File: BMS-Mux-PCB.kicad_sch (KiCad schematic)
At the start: 54 parts, among them J1 Conn_02x08_Counter_Clockwise, J2 Conn_02x08_Counter_Clockwise, J3 Conn_02x09_Top_Bottom, J4 Conn_01x18, J5 Conn_01x02, J6 Conn_02x10_Odd_Even, Q1 BSS123, Q2 BSS123, U1 74CBTLV3257, U2 74CBTLV3257, U3 TEC2-4812WI, U4 TEC2-4810WI

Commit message: V1 almost done - touching up silkscreen
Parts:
- renumbered F16 to F1, F7 to F10, F6 to F11, F5 to F12, F4 to F13, F3 to F14, F2 to F15, F1 to F16, F15 to F2, F14 to F3, F13 to F4, F12 to F5, F11 to F6, F10 to F7, F9 to F8, F8 to F9
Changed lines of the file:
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@@
 		(on_board yes)
 		(dnp no)
-		(property "Reference" "F13"
+		(property "Reference" "F4"
 			(at 99.06 189.484 90)
 			(effects
@@
 			(project "BMS-Mux-PCB"
 				(path "/a2925814-5dc3-4888-bdb8-1bf38cbb6bf2"
-					(reference "F13")
+					(reference "F4")
 					(unit 1)
 				)
@@
 		(on_board yes)
 		(dnp no)
-		(property "Reference" "F9"
+		(property "Reference" "F8"
 			(at 99.06 179.324 90)
 			(effects
@@
 			(project "BMS-Mux-PCB"
 				(path "/a2925814-5dc3-4888-bdb8-1bf38cbb6bf2"
-					(reference "F9")
+					(reference "F8")
 					(unit 1)
 				)
@@
 		(on_board yes)
 		(dnp no)
-		(property "Reference" "F11"
+		(property "Reference" "F6"
 			(at 99.06 184.404 90)
 			(effects
@@
 			(project "BMS-Mux-PCB"
 				(path "/a2925814-5dc3-4888-bdb8-1bf38cbb6bf2"
-					(reference "F11")
+					(reference "F6")
 					(unit 1)
 				)
@@
 		(on_board yes)
 		(dnp no)
-		(property "Reference" "F6"
+		(property "Reference" "F11"
 			(at 99.06 171.704 90)
 			(effects
@@
 			(project "BMS-Mux-PCB"
 				(path "/a2925814-5dc3-4888-bdb8-1bf38cbb6bf2"
-					(reference "F6")
+					(reference "F11")
 					(unit 1)
 				)
@@
 		(on_board yes)
 		(dnp no)
-		(property "Reference" "F16"
+		(property "Reference" "F1"
 			(at 99.06 197.104 90)
 			(effects
@@
 			(project "BMS-Mux-PCB"
 				(path "/a2925814-5dc3-4888-bdb8-1bf38cbb6bf2"
-					(reference "F16")
+					(reference "F1")
 					(unit 1)
 				)
@@
 		(on_board yes)
 		(dnp no)
-		(property "Reference" "F8"
+		(property "Reference" "F9"
 			(at 99.06 176.784 90)
 			(effects
@@
 			(project "BMS-Mux-PCB"
 				(path "/a2925814-5dc3-4888-bdb8-1bf38cbb6bf2"
-					(reference "F8")
+					(reference "F9")
 					(unit 1)
 				)
@@
 		(on_board yes)
 		(dnp no)
-		(property "Reference" "F1"
+		(property "Reference" "F16"
 			(at 99.06 159.004 90)
 			(effects
@@
 			(project "BMS-Mux-PCB"
 				(path "/a2925814-5dc3-4888-bdb8-1bf38cbb6bf2"
-					(reference "F1")
+					(reference "F16")
 					(unit 1)
 				)
@@
 		(on_board yes)
 		(dnp no)
-		(property "Reference" "F7"
+		(property "Reference" "F10"
 			(at 99.06 174.244 90)
 			(effects
@@
 			(project "BMS-Mux-PCB"
 				(path "/a2925814-5dc3-4888-bdb8-1bf38cbb6bf2"
-					(reference "F7")
+					(reference "F10")
 					(unit 1)
 				)
@@
 		(on_board yes)
 		(dnp no)
-		(property "Reference" "F2"
+		(property "Reference" "F15"
 			(at 99.06 161.544 90)
 			(effects
@@
 			(project "BMS-Mux-PCB"
 				(path "/a2925814-5dc3-4888-bdb8-1bf38cbb6bf2"
-					(reference "F2")
+					(reference "F15")
 					(unit 1)
 				)
@@
 		(on_board yes)
 		(dnp no)
-		(property "Reference" "F5"
+		(property "Reference" "F12"
 			(at 99.06 169.164 90)
 			(effects
@@
 			(project "BMS-Mux-PCB"
 				(path "/a2925814-5dc3-4888-bdb8-1bf38cbb6bf2"
-					(reference "F5")
+					(reference "F12")
 					(unit 1)
 				)
@@
 		(on_board yes)
 		(dnp no)
-		(property "Reference" "F10"
+		(property "Reference" "F7"
 			(at 99.06 181.864 90)
 			(effects
@@
 			(project "BMS-Mux-PCB"
 				(path "/a2925814-5dc3-4888-bdb8-1bf38cbb6bf2"
-					(reference "F10")
+					(reference "F7")
 					(unit 1)
 				)
@@
 		(on_board yes)
 		(dnp no)
-		(property "Reference" "F14"
+		(property "Reference" "F3"
 			(at 99.06 192.024 90)
 			(effects
@@
 			(project "BMS-Mux-PCB"
 				(path "/a2925814-5dc3-4888-bdb8-1bf38cbb6bf2"
-					(reference "F14")
+					(reference "F3")
 					(unit 1)
 				)
@@
 		(on_board yes)
 		(dnp no)
-		(property "Reference" "F3"
+		(property "Reference" "F14"
 			(at 99.06 164.084 90)
 			(effects
@@
 			(project "BMS-Mux-PCB"
 				(path "/a2925814-5dc3-4888-bdb8-1bf38cbb6bf2"
-					(reference "F3")
+					(reference "F14")
 					(unit 1)
 				)
@@
 		(on_board yes)
 		(dnp no)
-		(property "Reference" "F4"
+		(property "Reference" "F13"
 			(at 99.06 166.624 90)
 			(effects
@@
 			(project "BMS-Mux-PCB"
 				(path "/a2925814-5dc3-4888-bdb8-1bf38cbb6bf2"
-					(reference "F4")
+					(reference "F13")
 					(unit 1)
 				)
@@
 		(on_board yes)
 		(dnp no)
-		(property "Reference" "F15"
+		(property "Reference" "F2"
 			(at 99.06 194.564 90)
 			(effects
@@
 			(project "BMS-Mux-PCB"
 				(path "/a2925814-5dc3-4888-bdb8-1bf38cbb6bf2"
-					(reference "F15")
+					(reference "F2")
 					(unit 1)
 				)
@@
 		(on_board yes)
 		(dnp no)
-		(property "Reference" "F12"
+		(property "Reference" "F5"
 			(at 99.06 186.944 90)
 			(effects
@@
 			(project "BMS-Mux-PCB"
 				(path "/a2925814-5dc3-4888-bdb8-1bf38cbb6bf2"
-					(reference "F12")
+					(reference "F5")
 					(unit 1)
 				)

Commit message: added some small changes for manufacturing purposes and gerber file generated
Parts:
- C1, C2: Manufacturer Part Number (none) -> CL10B104KB85PND
- C3, C4: Manufacturer Part Number (none) -> 885382208016
- F1, F10, F11, F12, F13, F14, F15, F16, F2, F3, F4, F5, F6, F7, F8, F9: Manufacturer Part Number (none) -> 0466.250NR
- H1, H2, H3, H4: now not fitted
- J1, J2: Manufacturer Part Number (none) -> 43045-1600
- J3: Manufacturer Part Number (none) -> 43045-1800
- J4: Manufacturer Part Number (none) -> 1945151 (x2)
- J5: Manufacturer Part Number (none) -> 43650-0200
- J6: Manufacturer Part Number (none) -> PH2-20-UA
- Q1, Q2: Manufacturer Part Number (none) -> BSS123L
- R1, R10, R11, R12, R13, R14, R15, R16, R2, R3, R4, R5, R6, R7, R8, R9: Manufacturer Part Number (none) -> ERA-6AEB681V
- R17, R18: Manufacturer Part Number (none) -> ERA-6AEB163V
- U1, U2: Manufacturer Part Number (none) -> SN74LV4053ADR
- U3: Manufacturer Part Number (none) -> TEC2-4812WI
- U4: Manufacturer Part Number (none) -> TEC2-4810WI
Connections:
- net +12V_ISO: now reaches J5.1 (Pin_1), U3.6 (+VOUT)
- net GND_ISO: now reaches J5.2 (Pin_2), U3.7 (-VOUT)
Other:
- moved on the sheet: J5

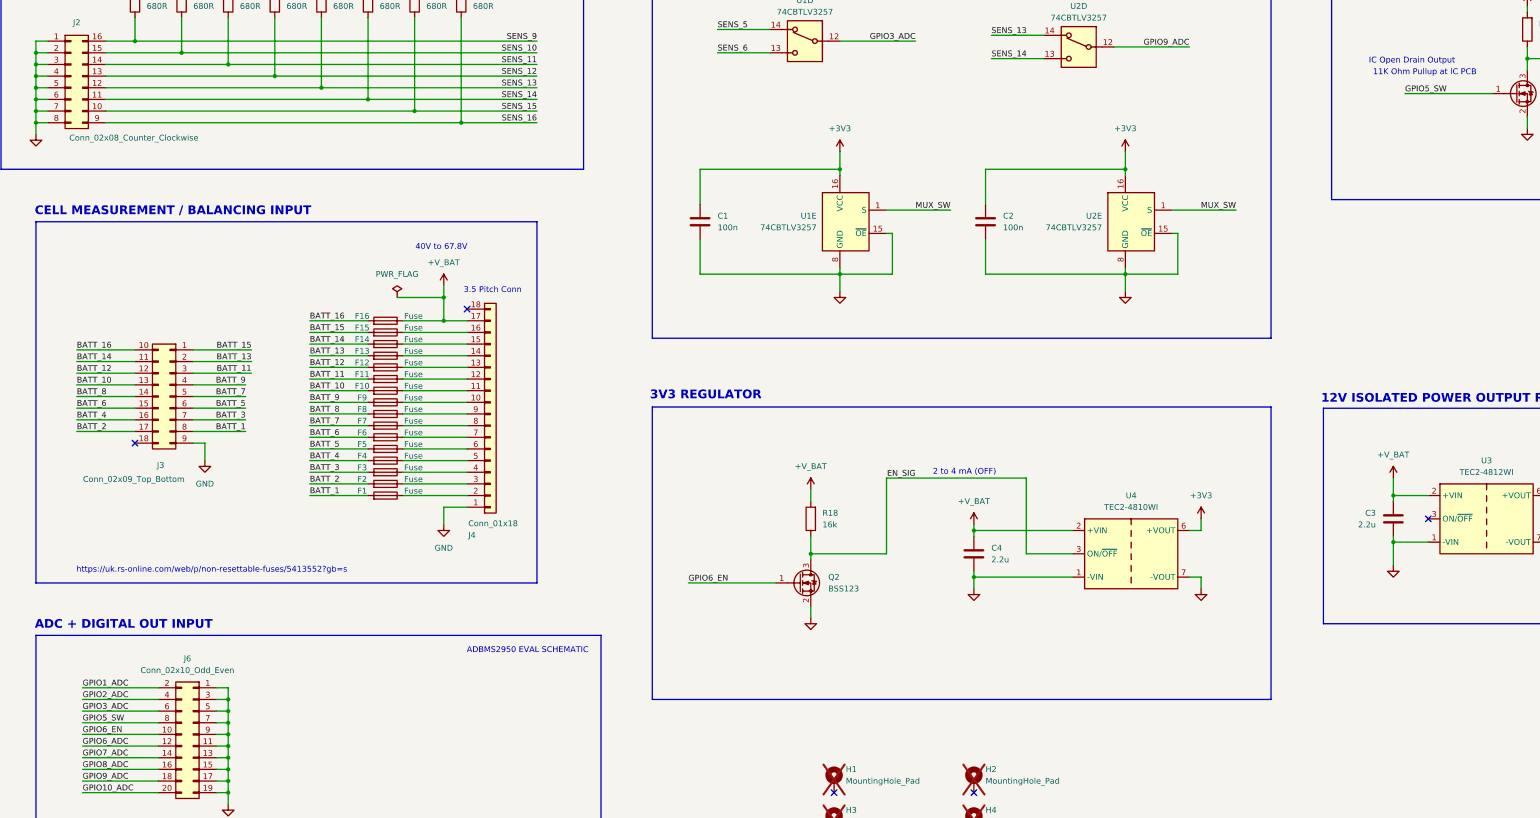
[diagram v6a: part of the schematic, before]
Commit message: fixed the gpio pin name number (minor fix)
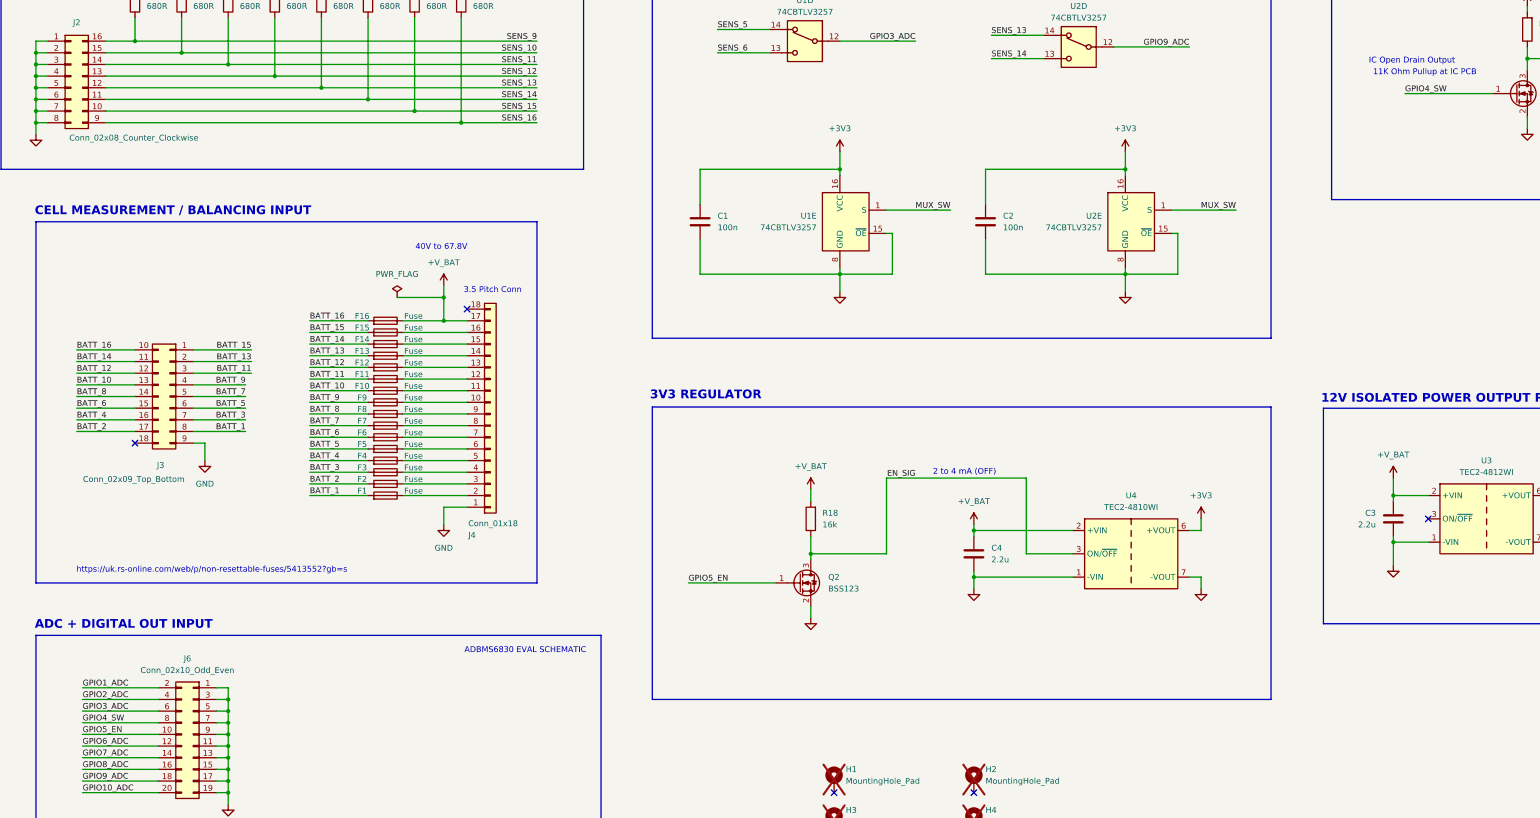
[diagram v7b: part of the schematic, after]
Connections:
- net GPIO5_SW renamed GPIO4_SW
- net GPIO6_EN renamed GPIO5_EN
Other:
- note added: "ADBMS6830 EVAL SCHEMATIC"
- note removed: "ADBMS2950 EVAL SCHEMATIC"
- title: (none) -> BMS MUX PCB
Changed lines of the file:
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@@
 	(generator_version "8.0")
 	(paper "A3")
+	(title_block
+		(title "BMS MUX PCB")
+		(rev "1")
+	)
 	(junction
 		(at 69.85 104.14)
@@
 		)
 	)
-	(text "ADBMS2950 EVAL SCHEMATIC"
+	(text "ADBMS6830 EVAL SCHEMATIC"
 		(exclude_from_sim no)
-		(at 135.128 231.902 0)
+		(at 134.62 231.902 0)
 		(effects
 			(font
@@
 		)
 	)
-	(label "GPIO5_SW"
+	(label "GPIO4_SW"
 		(at 38.1 247.65 0)
 		(effects
@@
 		)
 	)
-	(label "GPIO5_SW"
+	(label "GPIO4_SW"
 		(at 326.39 110.49 0)
 		(effects
@@
 		)
 	)
-	(label "GPIO6_EN"
+	(label "GPIO5_EN"
 		(at 170.18 217.17 0)
 		(effects
@@
 		)
 	)
-	(label "GPIO6_EN"
+	(label "GPIO5_EN"
 		(at 38.1 250.19 0)
 		(effects

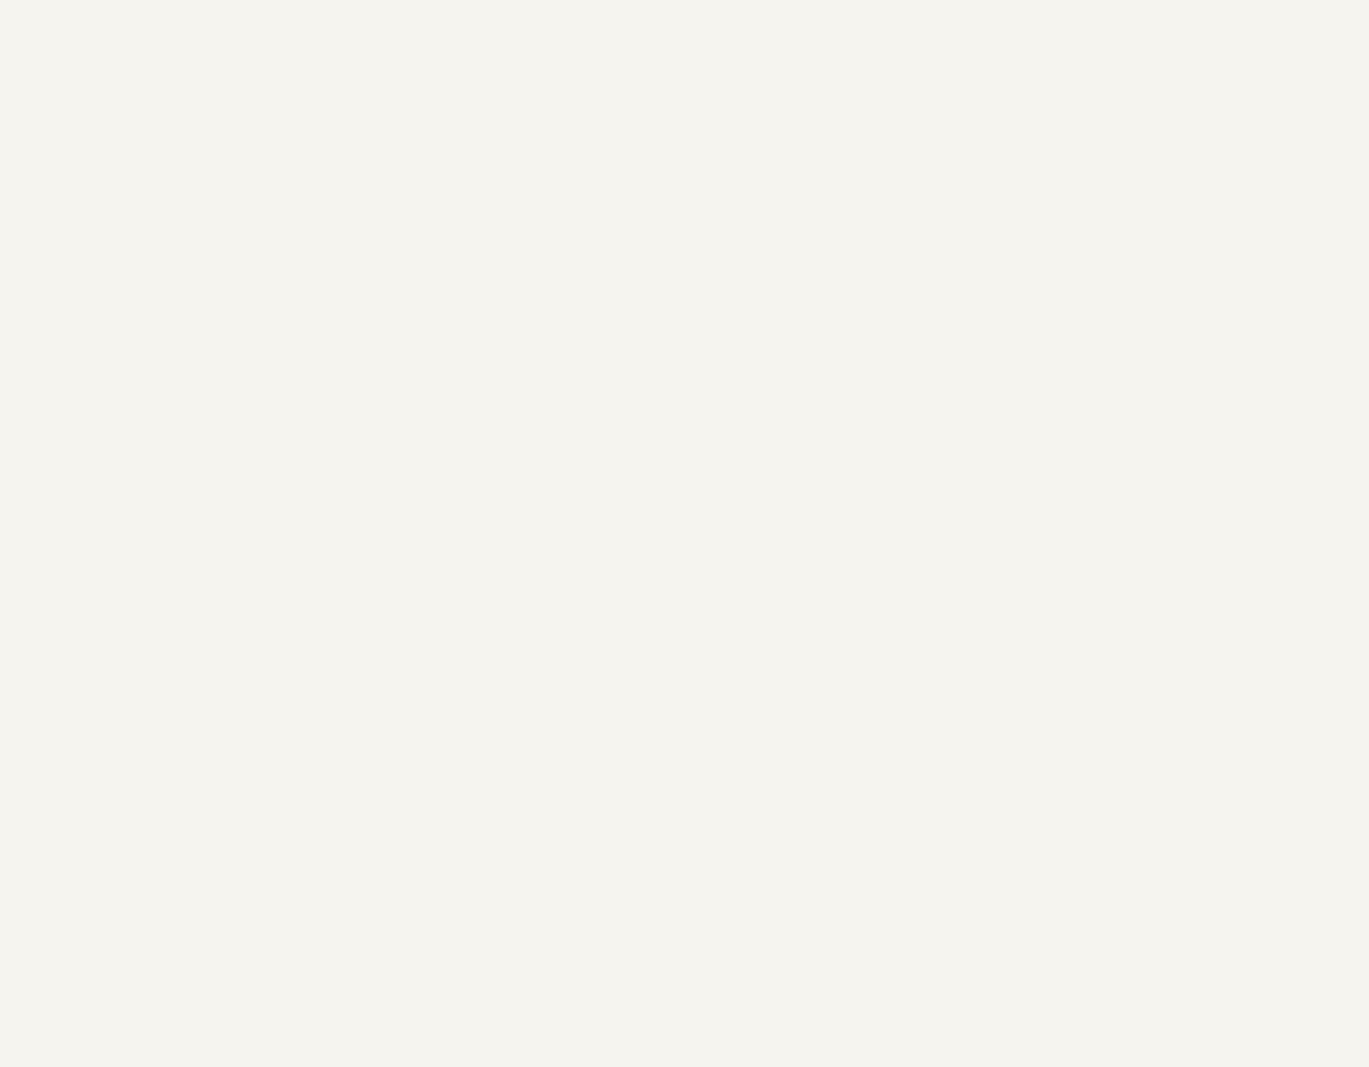
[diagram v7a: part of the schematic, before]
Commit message: added gitignore
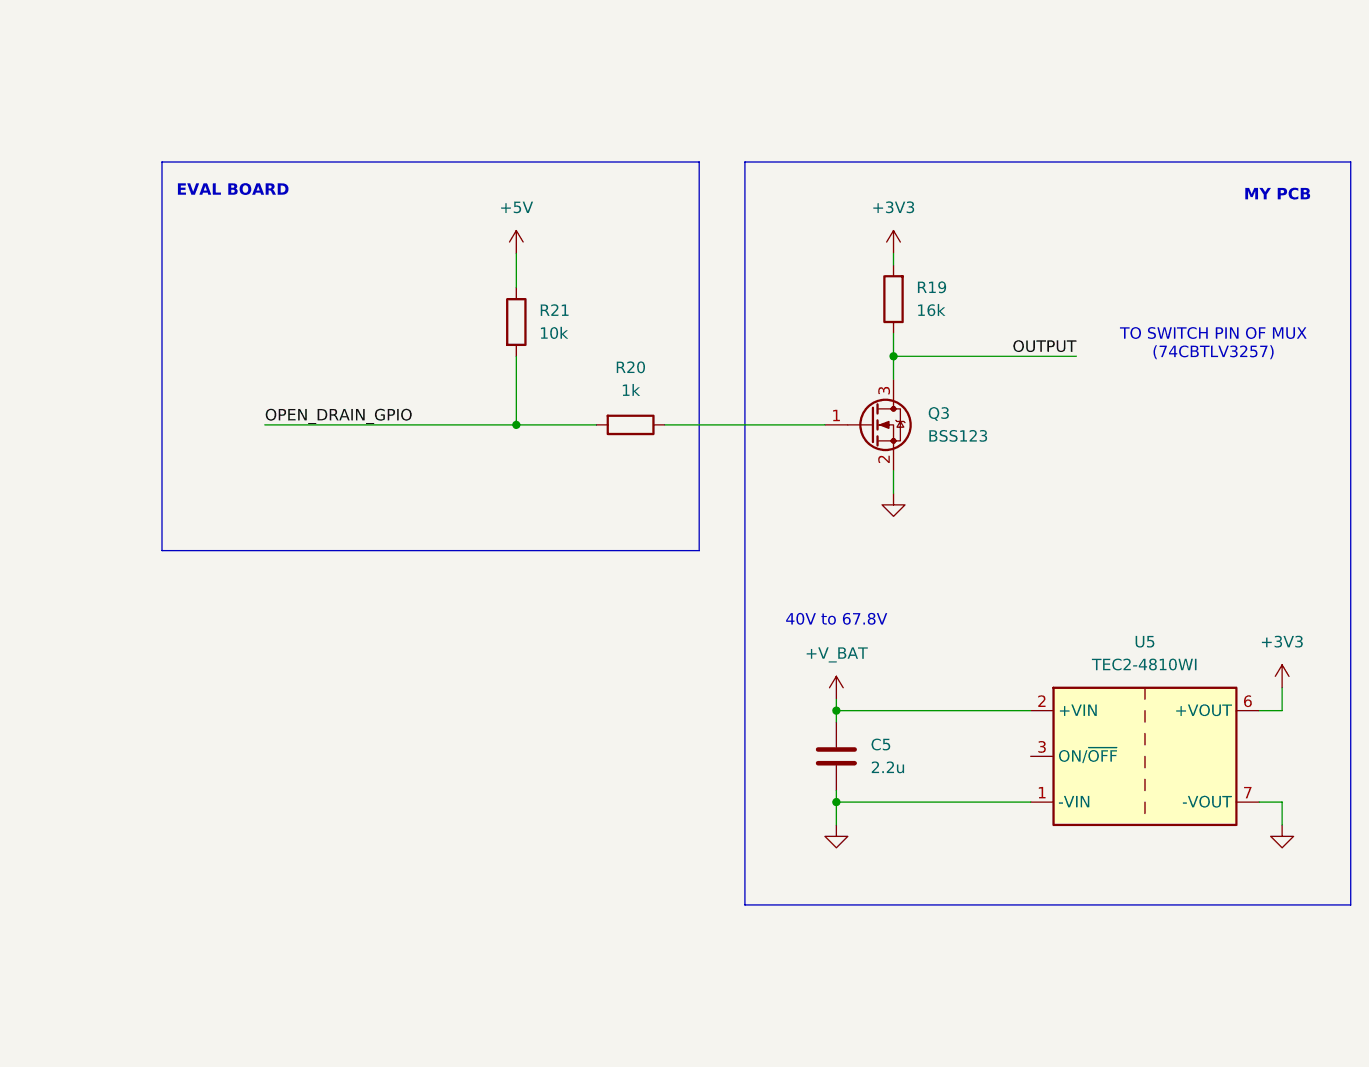
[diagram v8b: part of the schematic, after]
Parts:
- added C5: 2.2u, Capacitor_SMD:C_1206_3216Metric_Pad1.33x1.80mm_HandSolder, symbol Device:C
- added Q3: BSS123, Package_TO_SOT_SMD:SOT-23, symbol Transistor_FET:BSS123
- added R19: 16k, Resistor_SMD:R_0805_2012Metric, symbol Device:R
- added R20: 1k, Resistor_SMD:R_0805_2012Metric, symbol Device:R
- added R21: 10k, Resistor_SMD:R_0805_2012Metric, symbol Device:R
- added U5: TEC2-4810WI, Converter_DCDC:Converter_DCDC_TRACO_TMR-xxxx_THT, symbol Converter_DCDC:TEC2-4810WI
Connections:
- net +3V3: now also R19.2, U5.6 (+VOUT)
- net +V_BAT: now also C5.1, U5.2 (+VIN)
- net GND: now also C5.2, Q3.2 (S), U5.1 (-VIN), U5.7 (-VOUT)
- new net: Q3.1 (G), R20.1
- new net +5V: R21.1
- new net OPEN_DRAIN_GPIO: R20.2, R21.2
- new net OUTPUT: Q3.3 (D), R19.1
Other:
- note added: "EVAL BOARD"
- note added: "MY PCB"
- note added: "TO SWITCH PIN OF MUX (74CBTLV3257)"
